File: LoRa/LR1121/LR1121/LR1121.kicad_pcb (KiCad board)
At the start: 4 copper layers, 50 x 85 mm, 58 parts, among them J1 USB_B_Micro, J2 Con_GPS, SW1 NRST, SW2 BOOT0, U1 LBAA0XV2GT, U2 STM32L552CCUx, U3 MT29F4G01ABAFDWB-IT:F TR, U4 PCMF1USB3S, U5 MAX-M10S, U7 BQ25619ERTWR, Y1 32.768KHz, Y2 25MHz

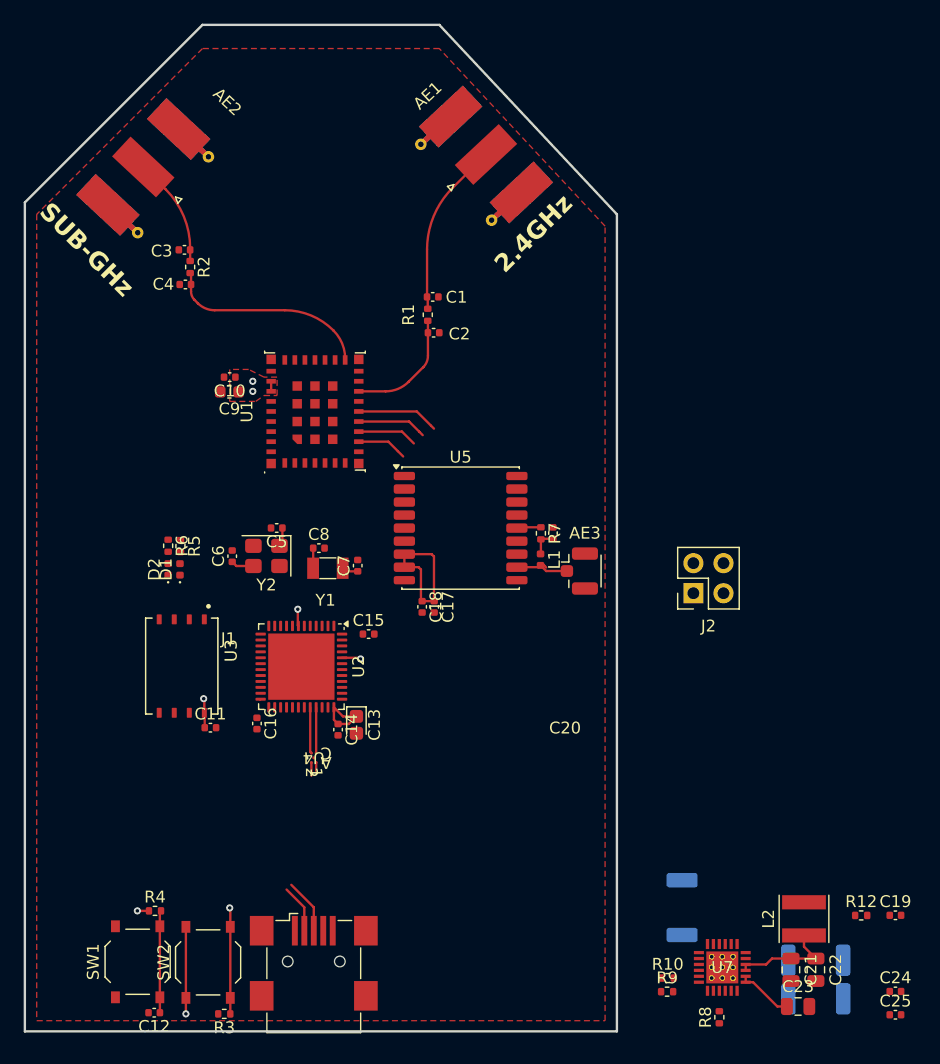
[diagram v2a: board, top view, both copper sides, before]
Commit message: [BB_IMX8ML] Change MCU F280015x
Change MCU STM32H5 for F2800157 dual core real-time
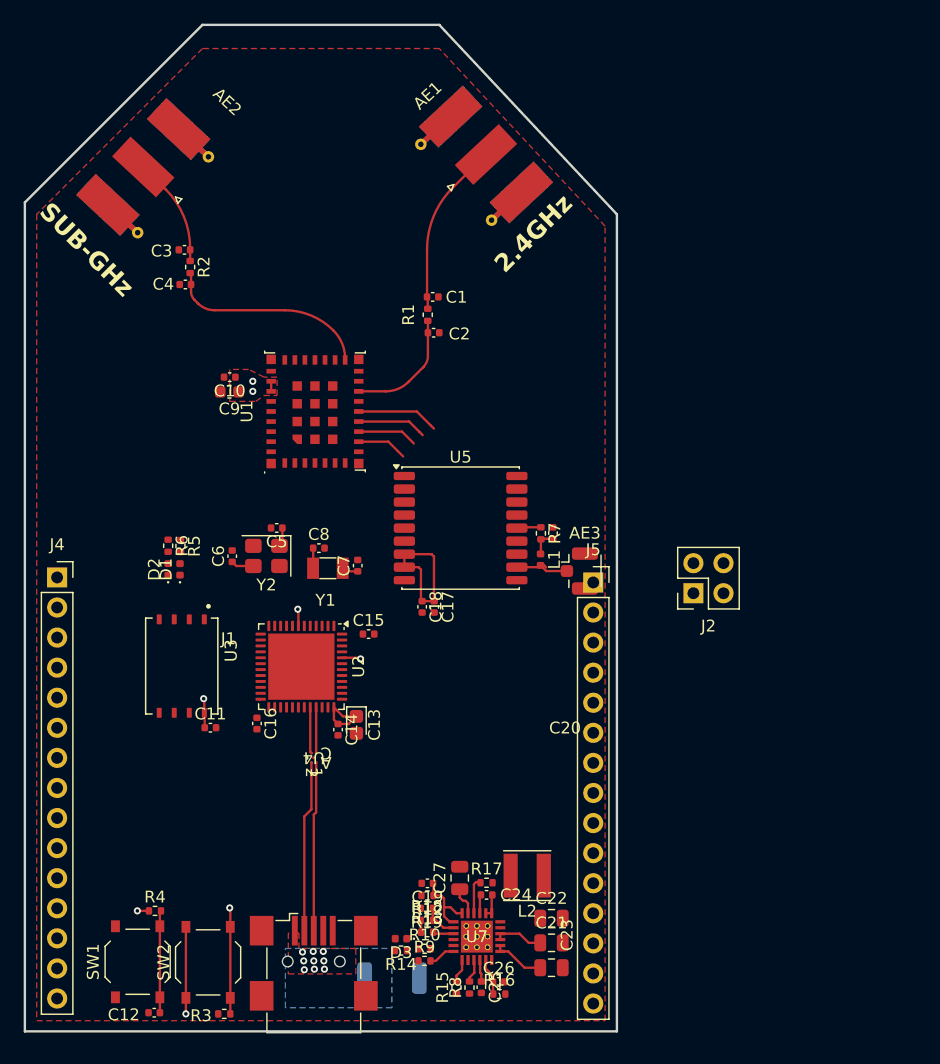
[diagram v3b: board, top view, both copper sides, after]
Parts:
- added C26: 0.1uF, Capacitor_SMD:C_0402_1005Metric, F.Cu at (140.0, 169.8)
- added C27: 10uF, Capacitor_SMD:C_0805_2012Metric, F.Cu at (136.7, 161.1)
- added D3: GREEN, LED_SMD:LED_0402_1005Metric, F.Cu at (131.8, 166.2)
- added J4: Conn_01x15_Pin, Connector_PinSocket_2.54mm:PinSocket_1x15_P2.54mm_Vertical, F.Cu at (102.7, 135.7)
- added J5: Conn_01x15_Pin, Connector_PinSocket_2.54mm:PinSocket_1x15_P2.54mm_Vertical, F.Cu at (148.0, 136.1)
- added R15: 10K, Resistor_SMD:R_0402_1005Metric, F.Cu at (136.4, 170.3)
- added R16: 10K, Resistor_SMD:R_0402_1005Metric, F.Cu at (140.1, 170.8)
- added R17: 10K, Resistor_SMD:R_0402_1005Metric, F.Cu at (139.0, 161.4)
- added R18: 2.21K, Resistor_SMD:R_0402_1005Metric, F.Cu at (133.9, 164.6)
- added R19: 0, Resistor_SMD:R_0402_1005Metric, F.Cu at (133.9, 163.6)
- R13: value 0.01 -> 2.21K; footprint Resistor_SMD:R_2010_5025Metric -> Resistor_SMD:R_0402_1005Metric; moved to F.Cu
- R14: value 0.01 -> 2.2K; footprint Resistor_SMD:R_2010_5025Metric -> Resistor_SMD:R_0402_1005Metric; moved to F.Cu
- moved C19 39.6 mm to (134.0, 161.5), turned to 180 degrees
- moved R12 36.7 mm to (134.0, 162.5), turned to 180 degrees
- moved C24 35.5 mm to (139.0, 162.5), turned to 180 degrees
- moved C25 35.0 mm to (138.6, 170.3), turned to -90 degrees
- moved R14 35.0 mm to (131.8, 167.2), turned to 180 degrees
- moved R13 33.3 mm to (134.0, 165.6)
- moved R11 25.2 mm to (131.0, 169.5), turned to 0 degrees
- moved L2 23.7 mm to (142.4, 160.8), turned to 180 degrees
- moved C22 22.7 mm to (144.5, 164.4), turned to 0 degrees
- moved R8 21.2 mm to (137.6, 170.3)
- moved C23 21.1 mm to (144.5, 168.6)
- moved U7 20.9 mm to (138.2, 166.0)
- moved R10 20.7 mm to (133.8, 167.0)
- moved R9 20.7 mm to (133.8, 168.1)
- moved C21 20.4 mm to (144.5, 166.5), turned to 0 degrees
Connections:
- net /LoRa-system/BOOT0 renamed /LoRa-system/ControlUnit/BOOT0
- net /LoRa-system/D1 renamed /LoRa-system/ControlUnit/D1
- net /LoRa-system/D2 renamed /LoRa-system/ControlUnit/D2
- net /LoRa-system/I2C-SCL_GPS renamed /LoRa-system/ComunicationUnit/I2C-SCL_GPS
- net /LoRa-system/I2C-SDA_GPS renamed /LoRa-system/ComunicationUnit/I2C-SDA_GPS
- net /LoRa-system/LoRa_BUSY renamed /LoRa-system/ComunicationUnit/LoRa_BUSY
- net /LoRa-system/LoRa_MISO renamed /LoRa-system/ComunicationUnit/LoRa_MISO
- net /LoRa-system/LoRa_MOSI renamed /LoRa-system/ComunicationUnit/LoRa_MOSI
- net /LoRa-system/LoRa_NRST renamed /LoRa-system/ComunicationUnit/LoRa_NRST
- net /LoRa-system/LoRa_NSS renamed /LoRa-system/ComunicationUnit/LoRa_NSS
- net /LoRa-system/LoRa_SCK renamed /LoRa-system/ComunicationUnit/LoRa_SCK
- net /LoRa-system/Mem_MISO renamed /LoRa-system/ControlUnit/Mem_MISO
- net /LoRa-system/Mem_MOSI renamed /LoRa-system/ControlUnit/Mem_MOSI
- net /LoRa-system/Mem_NSS renamed /LoRa-system/ControlUnit/Mem_NSS
- net /LoRa-system/Mem_SCK renamed /LoRa-system/ControlUnit/Mem_SCK
- net /LoRa-system/NRST renamed /LoRa-system/ControlUnit/NRST
- net /LoRa-system/PC14 renamed /LoRa-system/ControlUnit/PC14
- net /LoRa-system/PC15 renamed /LoRa-system/ControlUnit/PC15
- net /LoRa-system/PH0 renamed /LoRa-system/ControlUnit/PH0
- net /LoRa-system/PH1 renamed /LoRa-system/ControlUnit/PH1
- net /LoRa-system/USB_D+ renamed /LoRa-system/ControlUnit/USB_D+
- net /LoRa-system/USB_D- renamed /LoRa-system/ControlUnit/USB_D-
- net /LoRa-system/VBAT renamed /LoRa-system/ControlUnit/VBAT
- net Net-(U7-CE_N) renamed /LoRa-system/PowerUnit/PMIC_CE#
- net Net-(U7-SCL) renamed /LoRa-system/PowerUnit/I2C_PMIC_SCL
- net Net-(U7-SDA) renamed /LoRa-system/PowerUnit/I2C_PMIC_SDA
- C21 pad 1: Net-(C21-Pad1) -> /LoRa-system/PowerUnit/V_SYS
- C22 pad 1: Net-(C21-Pad1) -> /LoRa-system/PowerUnit/V_SYS
- C23 pad 1: Net-(C23-Pad1) -> Net-(J3-Pin_1)
- C25 pad 1: Net-(U7-BATSNS) -> Net-(J3-Pin_1)
- J1 pad 1: /LoRa-system/VIN -> V_IN
- J2 pad 1: /LoRa-system/GPS_RX -> /LoRa-system/ComunicationUnit/GPS_RX
- J2 pad 3: /LoRa-system/GPS_TX -> /LoRa-system/ComunicationUnit/GPS_TX
- L2 pad 1: Net-(C21-Pad1) -> /LoRa-system/PowerUnit/V_SYS
- R10 pad 1: Net-(R10-Pad1) -> /LoRa-system/PowerUnit/3V3
- R11 pad 1: unconnected-(R11-Pad1) -> V_IN
- R13 pad 1: Net-(C23-Pad1) -> /LoRa-system/PowerUnit/REGN
- R13 pad 2: unconnected-(R13-Pad2) -> /LoRa-system/PowerUnit/PMID_GOOD
- R14 pad 1: Net-(C21-Pad1) -> /LoRa-system/PowerUnit/3V3
- R14 pad 2: unconnected-(R14-Pad2) -> Net-(D3-A)
- R8 pad 1: Net-(R10-Pad1) -> /LoRa-system/PowerUnit/3V3
- R9 pad 1: Net-(R10-Pad1) -> /LoRa-system/PowerUnit/3V3
- U2 pad 12: /LoRa-system/GPS_RX -> /LoRa-system/ControlUnit/GPS_RX
- U2 pad 13: /LoRa-system/GPS_TX -> /LoRa-system/ControlUnit/GPS_TX
- U7 pad 10: Net-(U7-BATSNS) -> Net-(J3-Pin_1)
- U7 pad 11: /LoRa-system/TS -> /LoRa-system/PowerUnit/TS
- U7 pad 12: unconnected-(U7-QON_N-Pad12) -> /LoRa-system/PowerUnit/QON_N
- U7 pad 13: Net-(C23-Pad1) -> Net-(J3-Pin_1)
- U7 pad 14: Net-(C23-Pad1) -> Net-(J3-Pin_1)
- U7 pad 15: Net-(C21-Pad1) -> /LoRa-system/PowerUnit/V_SYS
- U7 pad 16: Net-(C21-Pad1) -> /LoRa-system/PowerUnit/V_SYS
- U7 pad 2: unconnected-(U7-PSEL-Pad2) -> /LoRa-system/PowerUnit/PSEL
- U7 pad 22: /LoRa-system/REGN -> /LoRa-system/PowerUnit/REGN
- U7 pad 23: unconnected-(U7-PMID-Pad23) -> /LoRa-system/PowerUnit/PMID
- U7 pad 3: unconnected-(U7-PMID_GOOD-Pad3) -> /LoRa-system/PowerUnit/PMID_GOOD
- U7 pad 4: unconnected-(U7-STAT-Pad4) -> /LoRa-system/PowerUnit/STAT
- U7 pad 7: /LoRa-system/INT_N -> /LoRa-system/PowerUnit/INT_N
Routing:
- net Net-(J1-D-): track 5.20 -> 14.4 mm
- net Net-(C21-Pad1): track 9.00 -> 0.00 mm
- net Net-(J1-D+): track 5.36 -> 14.3 mm
- net Net-(U7-VAC): track 0.00 -> 6.26 mm
- net Net-(J3-Pin_1): track 0.00 -> 6.14 mm
- net Net-(C23-Pad1): track 4.82 -> 0.00 mm
- net /LoRa-system/PowerUnit/V_SYS: track 0.00 -> 4.20 mm
- net /LoRa-system/PowerUnit/REGN: track 0.00 -> 4.16 mm
- net /LoRa-system/PowerUnit/TS: track 0.00 -> 3.14 mm
- net /LoRa-system/PowerUnit/PSEL: track 0.00 -> 3.02 mm
- net /LoRa-system/PowerUnit/I2C_PMIC_SDA: track 0.00 -> 2.51 mm
- net /LoRa-system/PowerUnit/PMID: track 0.00 -> 2.45 mm
- net Net-(C24-Pad1): track 0.00 -> 2.07 mm
- net /LoRa-system/PowerUnit/INT_N: track 0.00 -> 2.00 mm
- net /LoRa-system/PowerUnit/PMIC_CE#: track 0.00 -> 1.82 mm
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- added copper zone on B.Cu, net V_IN
- added copper zone on F.Cu, net V_IN

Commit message: [IMX8ML] Add new layer
A new layers was add in the cpu schematic, now it had 8 layer.
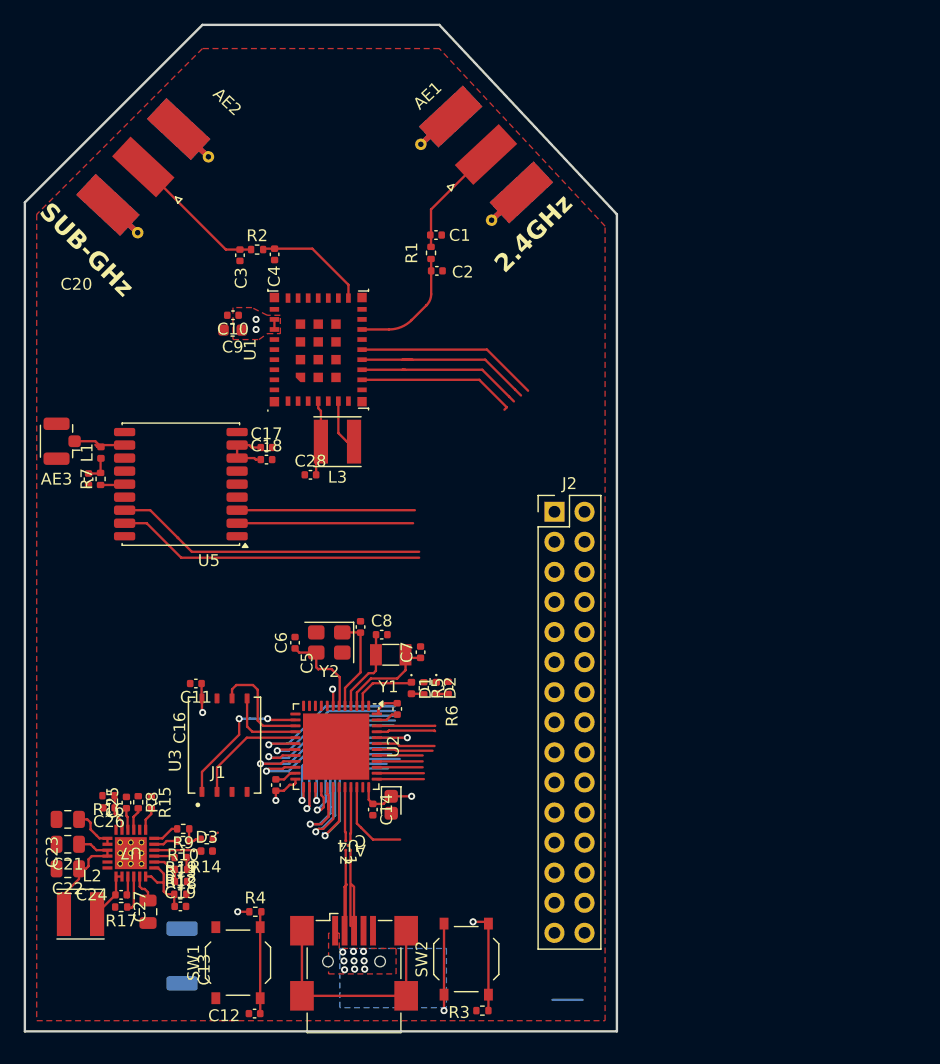
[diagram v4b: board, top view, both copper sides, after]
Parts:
- removed J4, J5: Conn_01x15_Pin, Connector_PinSocket_2.54mm:PinSocket_1x15_P2.54mm_Vertical
- added C28: 470nF, Capacitor_SMD:C_0402_1005Metric, F.Cu at (124.1, 127.0)
- added L3: 15uH, Inductor_SMD:L_Taiyo-Yuden_MD-4040, F.Cu at (126.4, 124.2)
- J2: value Con_GPS -> PinOUT; footprint Connector_PinSocket_2.54mm:PinSocket_2x02_P2.54mm_Vertical -> Connector_PinHeader_2.54mm:PinHeader_2x15_P2.54mm_Vertical
- moved AE3 45.0 mm to (103.2, 124.2), turned to 180 degrees
- moved C23 42.7 mm to (103.6, 156.1), turned to 180 degrees
- moved C21 41.7 mm to (103.6, 158.2), turned to 180 degrees
- moved C22 41.1 mm to (103.6, 160.3), turned to 180 degrees
- moved C20 39.5 mm to (105.4, 127.4), turned to -90 degrees
- moved L1 38.2 mm to (106.4, 125.1), turned to 90 degrees
- moved L2 37.9 mm to (104.7, 164.1), turned to 0 degrees
- moved R7 37.5 mm to (106.4, 127.3), turned to 90 degrees
- moved R16 37.0 mm to (107.1, 154.1), turned to 180 degrees
- moved C26 36.0 mm to (107.1, 155.1), turned to 180 degrees
- moved C25 33.8 mm to (108.6, 154.7), turned to 90 degrees
- moved R8 32.1 mm to (109.6, 154.6), turned to -90 degrees
- moved R17 30.9 mm to (108.1, 163.5), turned to 180 degrees
- moved C24 30.9 mm to (108.1, 162.5), turned to 0 degrees
- moved R15 30.1 mm to (110.7, 154.7), turned to -90 degrees
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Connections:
- net /LoRa-system/ComunicationUnit/LoRa_BUSY renamed LoRa_BUSY
- net /LoRa-system/ComunicationUnit/LoRa_NRST renamed LoRa_NRST
- J2 pad 1: /LoRa-system/ComunicationUnit/GPS_RX -> +3.3V
- J2 pad 2: Net-(J2-Pin_2) -> +3.3V
- J2 pad 3: /LoRa-system/ComunicationUnit/GPS_TX -> I2CSCL_GPS
- J2 pad 4: Net-(J2-Pin_4) -> PA0
- R10 pad 2: /LoRa-system/PowerUnit/I2C_PMIC_SCL -> I2CSCL_GPS
- R9 pad 2: /LoRa-system/PowerUnit/I2C_PMIC_SDA -> I2CSDA_GPS
- U1 pad 1: unconnected-(U1-DIO9-Pad1) -> LoRa_Int
- U1 pad 10: /LoRa-system/ComunicationUnit/LoRa_NSS -> LoRa_NSS
- U1 pad 11: /LoRa-system/ComunicationUnit/LoRa_MISO -> LoRa_MISO
- U1 pad 12: /LoRa-system/ComunicationUnit/LoRa_MOSI -> LoRa_MOSI
- U1 pad 13: /LoRa-system/ComunicationUnit/LoRa_SCK -> LoRa_SCK
- U1 pad 2: unconnected-(U1-DIO8-Pad2) -> GND
- U1 pad 4: unconnected-(U1-VREG-Pad4) -> /LoRa-system/ComunicationUnit/VREG
- U1 pad 6: unconnected-(U1-DCC_SW-Pad6) -> Net-(U1-DCC_SW)
- U2 pad 10: unconnected-(U2-PA0-Pad10) -> PA0
- U2 pad 11: unconnected-(U2-PA1-Pad11) -> PA1
- U2 pad 12: /LoRa-system/ControlUnit/GPS_RX -> /LoRa-system/ControlUnit/MCU_Rx
- U2 pad 13: /LoRa-system/ControlUnit/GPS_TX -> /LoRa-system/ControlUnit/MCU_Tx
- U2 pad 14: unconnected-(U2-PA4-Pad14) -> /LoRa-system/ControlUnit/Mem_NSS
- U2 pad 15: unconnected-(U2-PA5-Pad15) -> /LoRa-system/ControlUnit/Mem_SCK
- U2 pad 16: unconnected-(U2-PA6-Pad16) -> /LoRa-system/ControlUnit/Mem_MISO
- U2 pad 17: unconnected-(U2-PA7-Pad17) -> /LoRa-system/ControlUnit/Mem_MOSI
- U2 pad 18: unconnected-(U2-PB0-Pad18) -> PB0
- U2 pad 19: unconnected-(U2-PB1-Pad19) -> PB1
- U2 pad 2: unconnected-(U2-PC13-Pad2) -> /LoRa-system/ControlUnit/D1
- U2 pad 20: unconnected-(U2-PB2-Pad20) -> PB2
- U2 pad 21: unconnected-(U2-PB10-Pad21) -> PB10
- U2 pad 22: unconnected-(U2-PB11-Pad22) -> PB11
- U2 pad 25: unconnected-(U2-PB12-Pad25) -> LoRa_NSS
- U2 pad 26: unconnected-(U2-PB13-Pad26) -> LoRa_SCK
- U2 pad 27: unconnected-(U2-PB14-Pad27) -> LoRa_MISO
- U2 pad 28: unconnected-(U2-PB15-Pad28) -> LoRa_MOSI
- U2 pad 29: unconnected-(U2-PA8-Pad29) -> PA8
- U2 pad 30: unconnected-(U2-PA9-Pad30) -> PA9
- U2 pad 31: unconnected-(U2-PA10-Pad31) -> PA10
- U2 pad 34: unconnected-(U2-PA13-Pad34) -> PA13
- U2 pad 37: unconnected-(U2-PA14-Pad37) -> PA14
- U2 pad 38: unconnected-(U2-PA15-Pad38) -> PA15
- U2 pad 39: unconnected-(U2-PB3-Pad39) -> PB3
- U2 pad 40: unconnected-(U2-PB4-Pad40) -> PB4
- U2 pad 41: unconnected-(U2-PB5-Pad41) -> PB5
- U2 pad 42: unconnected-(U2-PB6-Pad42) -> I2CSDA_GPS
- U2 pad 43: unconnected-(U2-PB7-Pad43) -> I2CSCL_GPS
- U2 pad 45: unconnected-(U2-PB8-Pad45) -> PB8
- U2 pad 46: unconnected-(U2-PB9-Pad46) -> PB9
- U5 pad 16: /LoRa-system/ComunicationUnit/I2C-SDA_GPS -> I2CSDA_GPS
- U5 pad 17: /LoRa-system/ComunicationUnit/I2C-SCL_GPS -> I2CSCL_GPS
- U5 pad 2: Net-(J2-Pin_4) -> GPS_TX
- U5 pad 3: Net-(J2-Pin_2) -> GPS_RX
- U7 pad 5: /LoRa-system/PowerUnit/I2C_PMIC_SCL -> I2CSCL_GPS
- U7 pad 6: /LoRa-system/PowerUnit/I2C_PMIC_SDA -> I2CSDA_GPS
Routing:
- net I2CSDA_GPS: track 0.00 -> 33.8 mm
- net I2CSCL_GPS: track 0.00 -> 33.1 mm
- net LoRa_SCK: track 0.00 -> 28.6 mm, vias 0 -> 1
- net LoRa_MOSI: track 0.00 -> 27.6 mm, vias 0 -> 1
- net LoRa_NSS: track 0.00 -> 25.8 mm, vias 0 -> 1
- net LoRa_MISO: track 0.00 -> 24.8 mm, vias 0 -> 1
- net unconnected-(J1-Shield-Pad6): track 0.00 -> 19.8 mm
- net PA8: track 0.00 -> 16.9 mm, vias 0 -> 1
- net PB10: track 0.00 -> 15.9 mm, vias 0 -> 1
- net GPS_RX: track 0.00 -> 15.0 mm
- net PB11: track 0.00 -> 14.9 mm, vias 0 -> 1
- net PA9: track 0.00 -> 14.9 mm, vias 0 -> 1
- net GPS_TX: track 0.00 -> 14.9 mm
- net PA10: track 0.00 -> 14.6 mm, vias 0 -> 1
- net PB2: track 0.00 -> 14.5 mm, vias 0 -> 1
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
